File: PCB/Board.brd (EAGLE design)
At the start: 21.4 x 42 mm, 15 parts, among them J1 PINHD-2X5, J2 PINHD-2X5, Q1 NMOSFET, Q2 NMOSFET, Q3 NMOSFET, Q4 NMOSFET

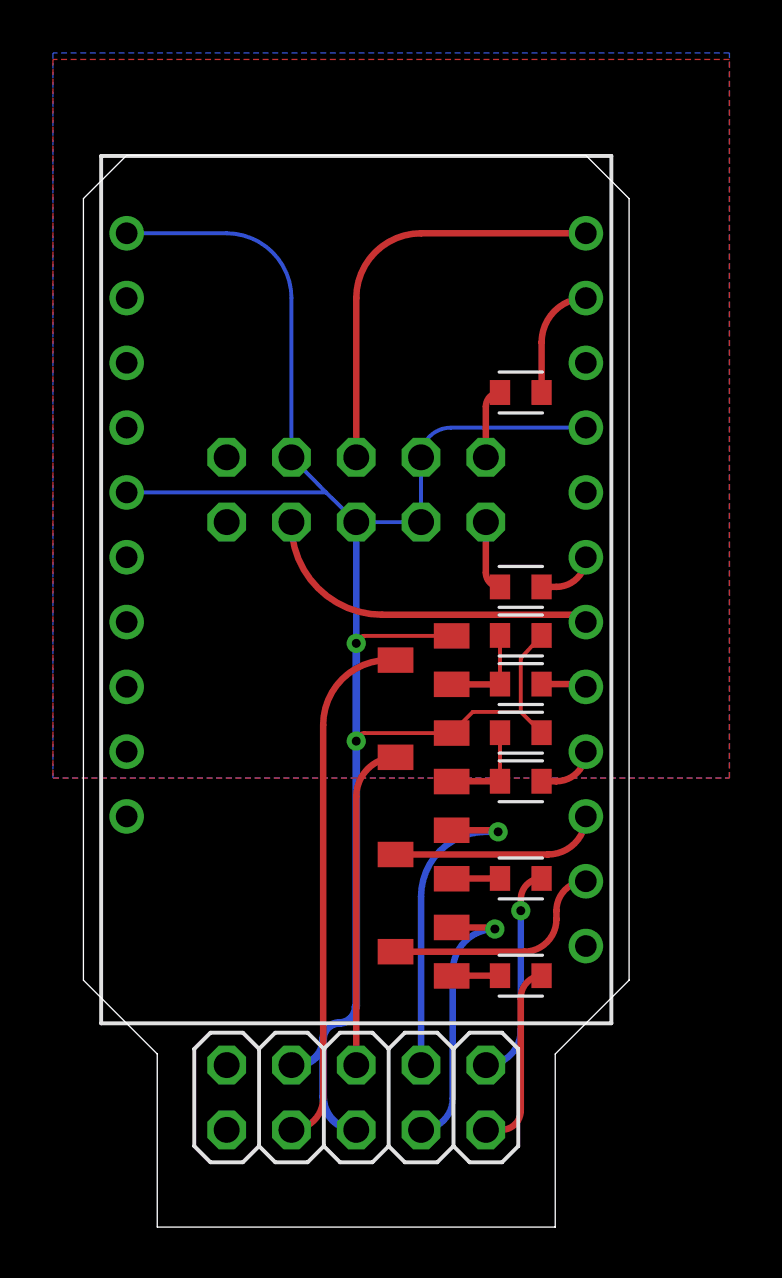
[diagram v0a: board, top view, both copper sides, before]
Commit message: 基板を更新: LEDを5Vから駆動するようにしたりRESET / HDDLEDを触らないようにしたり
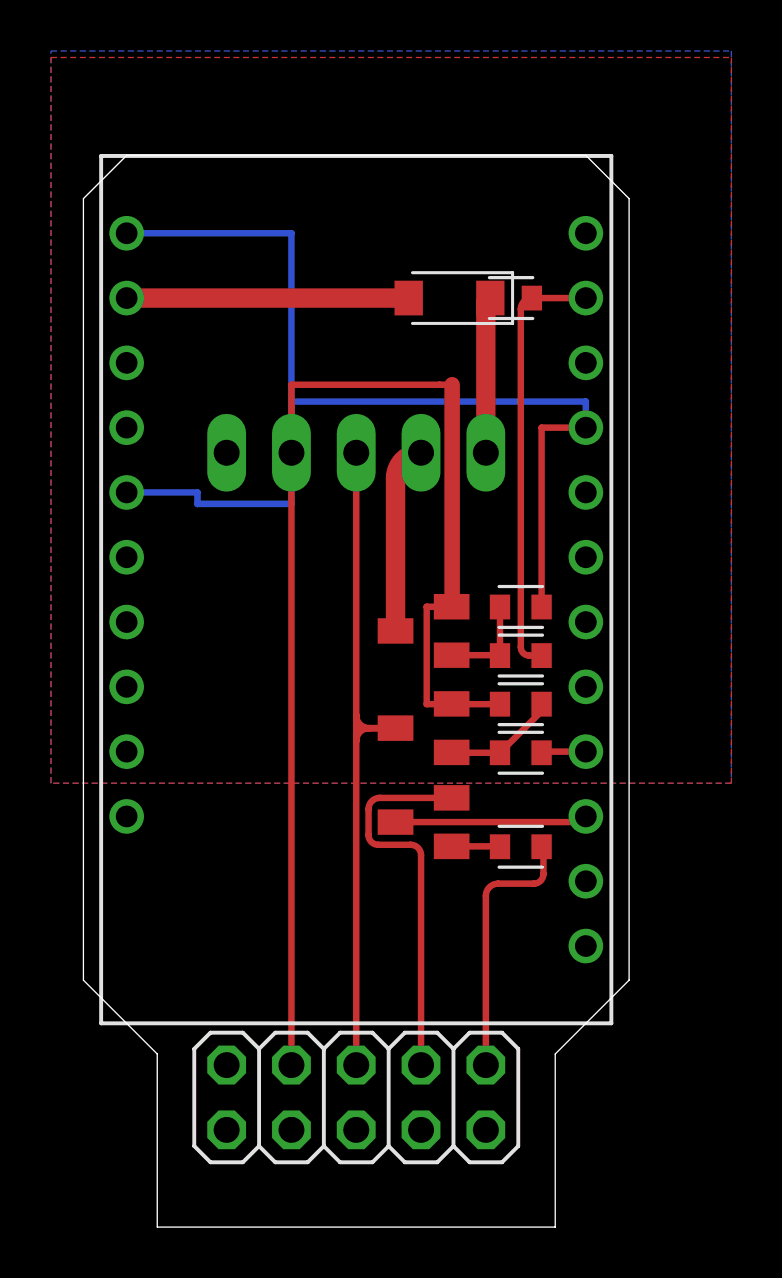
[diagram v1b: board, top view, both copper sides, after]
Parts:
- removed J2: PINHD-2X5, Connector:2X05
- removed Q4: NMOSFET, Transistor:SOT23
- removed R6, R8: (no value), Resistor:RESC1608X60
- added D2: DIODE, Diode:SODFL3718X115
- added JP1: PINHD-1X5, Connector:1X05
- moved Q2 12.6 mm to (13.3, 23.4)
- moved R3 3.72 mm to (16.8, 36.4), turned to 0 degrees
- moved Q1 1.27 mm to (13.3, 15.9)
- moved R5 1.24 mm to (17.1, 14.9)
- moved Q3 1.14 mm to (13.3, 19.6)
- moved R7 1.12 mm to (17.1, 20.5), turned to 0 degrees
- moved R1 1.12 mm to (17.1, 18.6)
- moved R2 1.12 mm to (17.1, 22.4)
- moved R4 0.79 mm to (17.1, 24.3)
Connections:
- removed net HD_LED+: J1.2, R6.2
- removed net HD_LED-: J1.4, Q2.2
- removed net HD_LED_CASE: R4.1, U$1.G10
- removed net HD_LED_MB: Q2.3, U$1.G4
- removed net N$3: J2.1, R4.2
- removed net N$6: Q2.1, R6.1
- removed net PWRBTN_CASE: J2.6, U$1.G0
- removed net RESET#: J1.8, Q4.3
- removed net RESETBTN_CASE: J2.7, U$1.G8
- removed net RESETBTN_MB: R2.2, U$1.G7
- new net PWR_LED_CASE_SW: R2.2, R3.2, U$1.G1
- new net VCC: D2.2, U$1.5V2
- net GND: now also JP1.4, Q2.2, R4.1; no longer J1.6, J2.3, J2.4, J2.5, J2.8, Q4.2, R8.1
- net N$2: now also Q2.1, R4.2; no longer Q4.1, R8.2
- net N$4: now also D2.1, JP1.1, R3.1; no longer J2.2, R3.2
- net PWRBTN#: now also JP1.3
- net PWR_LED_CASE: now also JP1.2, Q2.3; no longer R3.1, U$1.G1
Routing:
- net RESET#: track 20.3 -> 0.00 mm
- net GND: track 79.0 -> 96.7 mm, vias 2 -> 0
- net PWR_LED_CASE_SW: track 0.00 -> 16.9 mm
- net PWRBTN_CASE: track 16.3 -> 0.00 mm
- net PWRBTN#: track 12.7 -> 28.0 mm
- net RESETBTN_CASE: track 13.2 -> 0.00 mm
- net VCC: track 0.00 -> 11.1 mm
- net HD_LED-: track 10.8 -> 0.00 mm, vias 1 -> 0
- net HD_LED_MB: track 8.80 -> 0.00 mm
- net HD_LED+: track 7.28 -> 0.00 mm
- net N$4: track 2.77 -> 6.19 mm
- net PWR_LED_CASE: track 4.42 -> 7.40 mm
- net N$3: track 2.77 -> 0.00 mm
- net PWR_LED-: track 12.5 -> 15.1 mm, vias 1 -> 0
- net HD_LED_CASE: track 2.22 -> 0.00 mm
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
